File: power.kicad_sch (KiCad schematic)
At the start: 32 parts, among them J1 Conn_01x02, J2 XT30PB-M, J3 Conn_01x02, J4 Conn_01x02, Q1 IRF4905, U1 TSR3-24120N, U2 R-78E5.0-1.0, U3 TMCS1100A2QDR

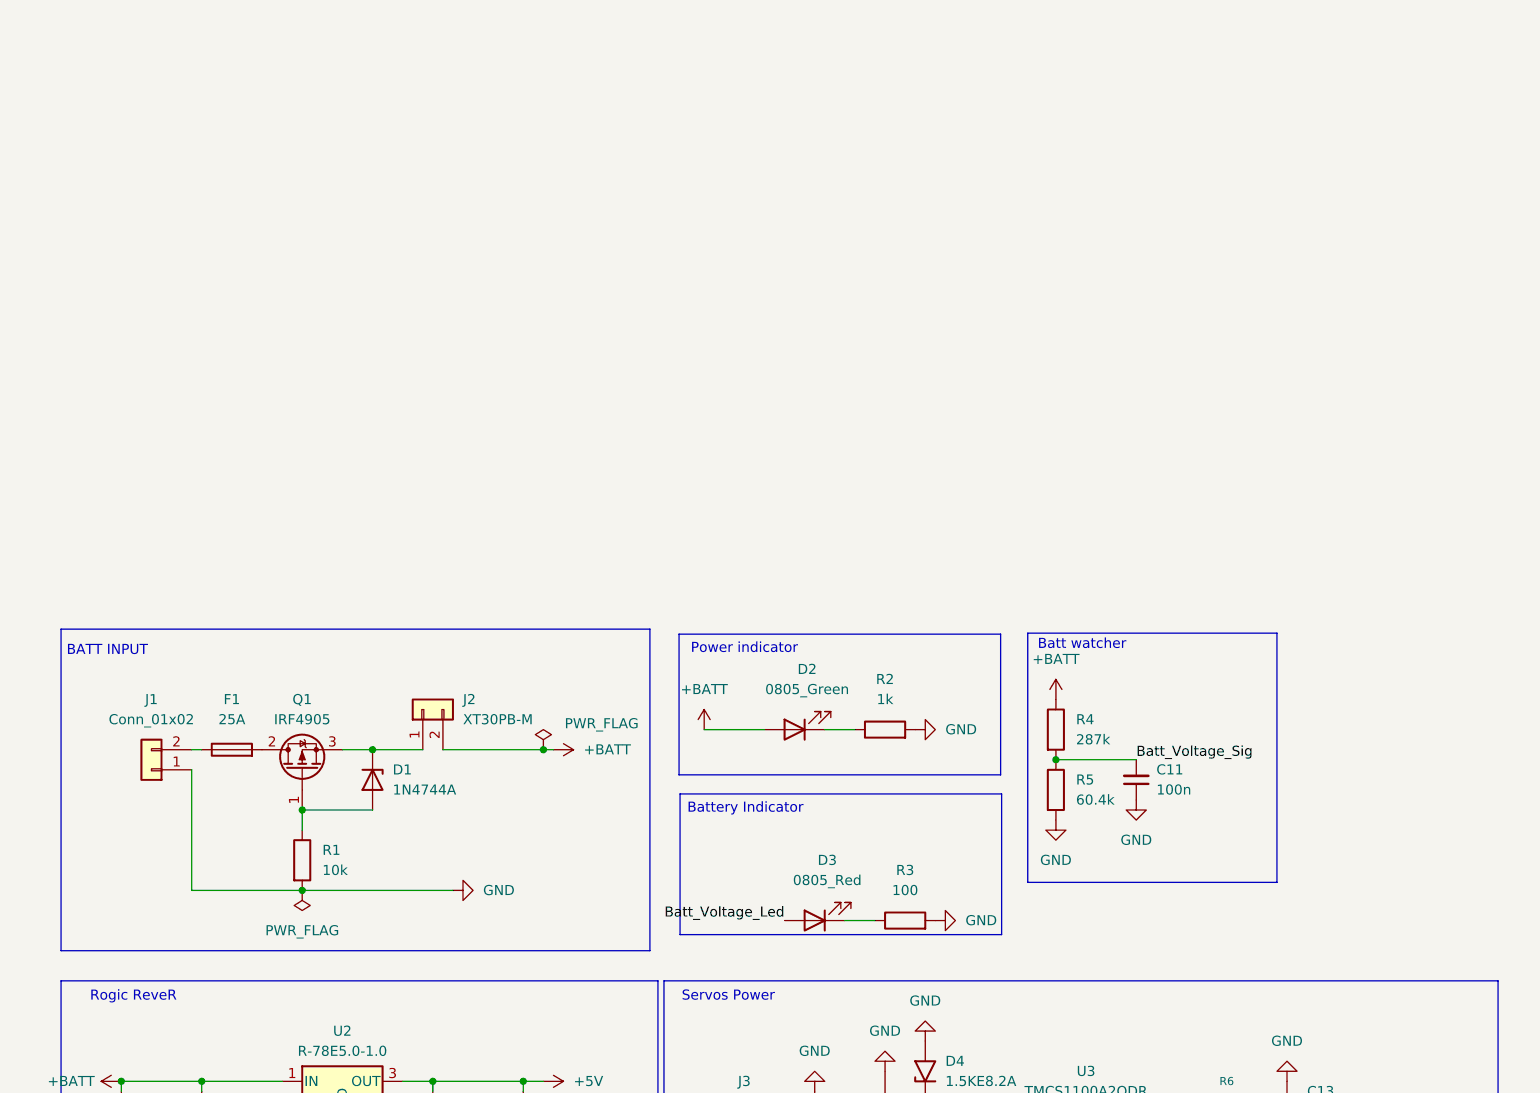
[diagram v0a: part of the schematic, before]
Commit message: Add relay for BAU + fixes
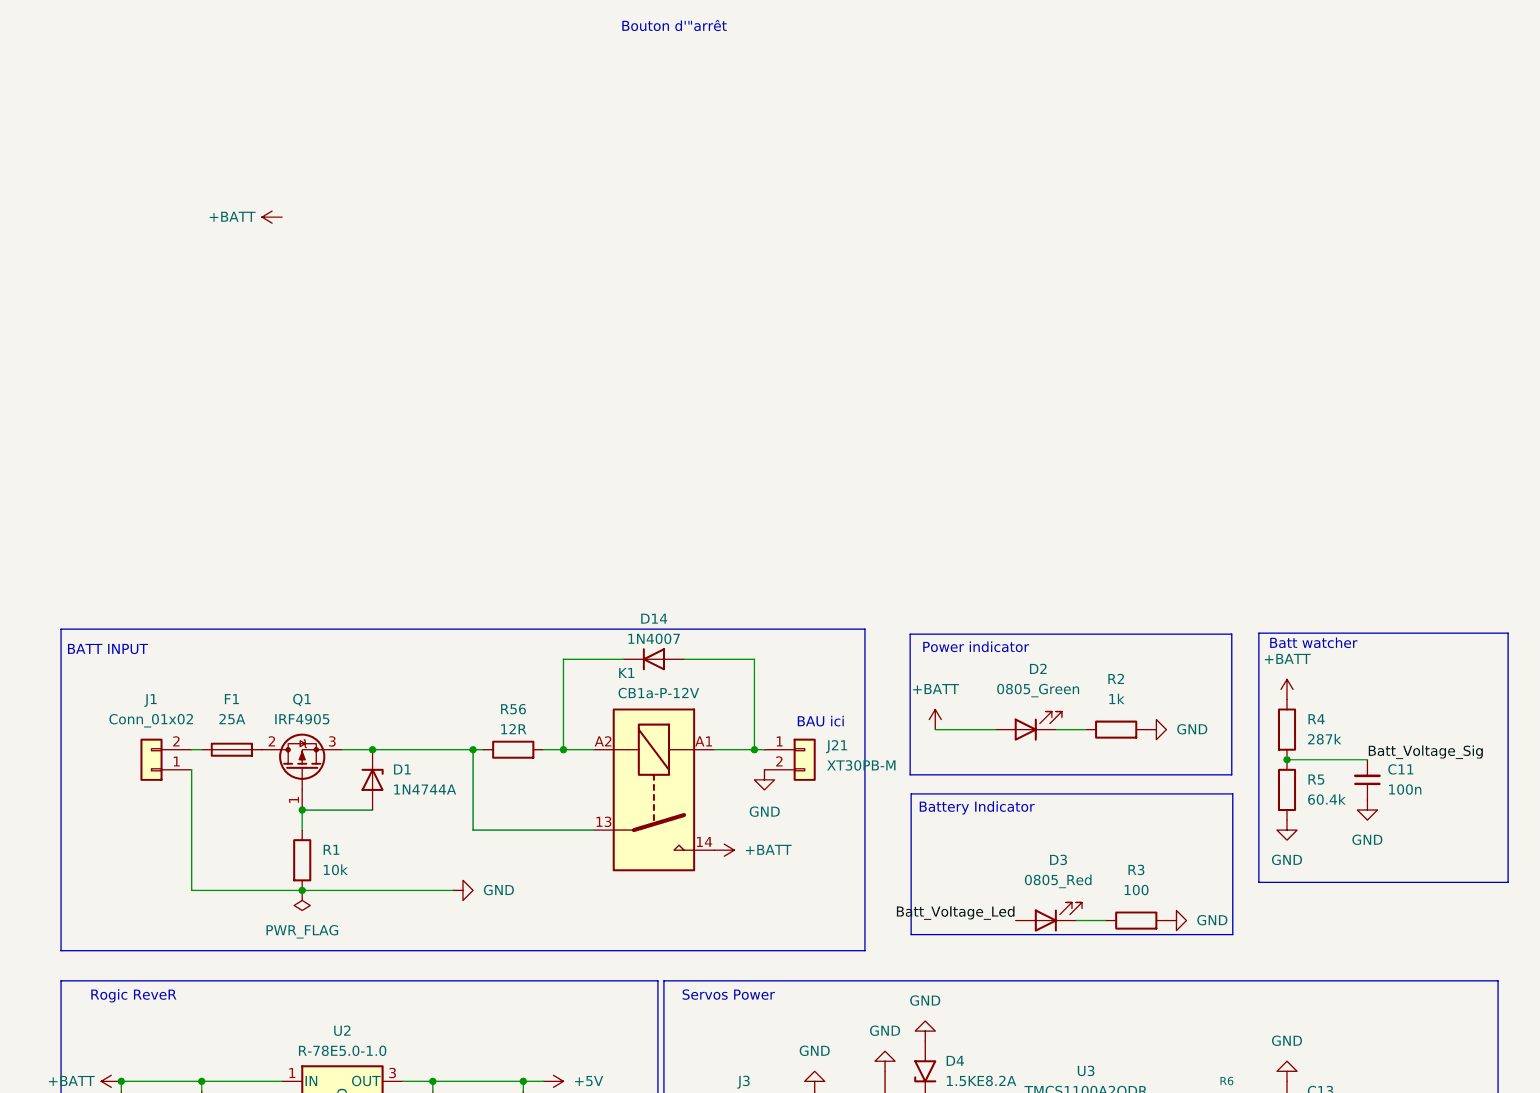
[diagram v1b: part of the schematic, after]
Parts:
- removed J2: XT30PB-M, symbol Connector_Generic:Conn_01x02
- added D14: 1N4007, symbol Device:D
- added J21: XT30PB-M, symbol Connector_Generic:Conn_01x02
- added K1: CB1a-P-12V, symbol Relay:Relay_SPST-NO
- added R56: 12R, symbol Device:R
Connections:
- net +BATT: now also K1.14
- net GND: now also J21.2 (Pin_2)
- net at D1.1 (K), Q1.3 (S): now also K1.13, R56.1
- new net: D14.2 (A), J21.1 (Pin_1), K1.A1
- new net: D14.1 (K), K1.A2, R56.2
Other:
- note added: "BAU ici"
- note added: "Bouton d'"arrêt"
- moved on the sheet: C11, D2, D3, R2, R3, R4, R5

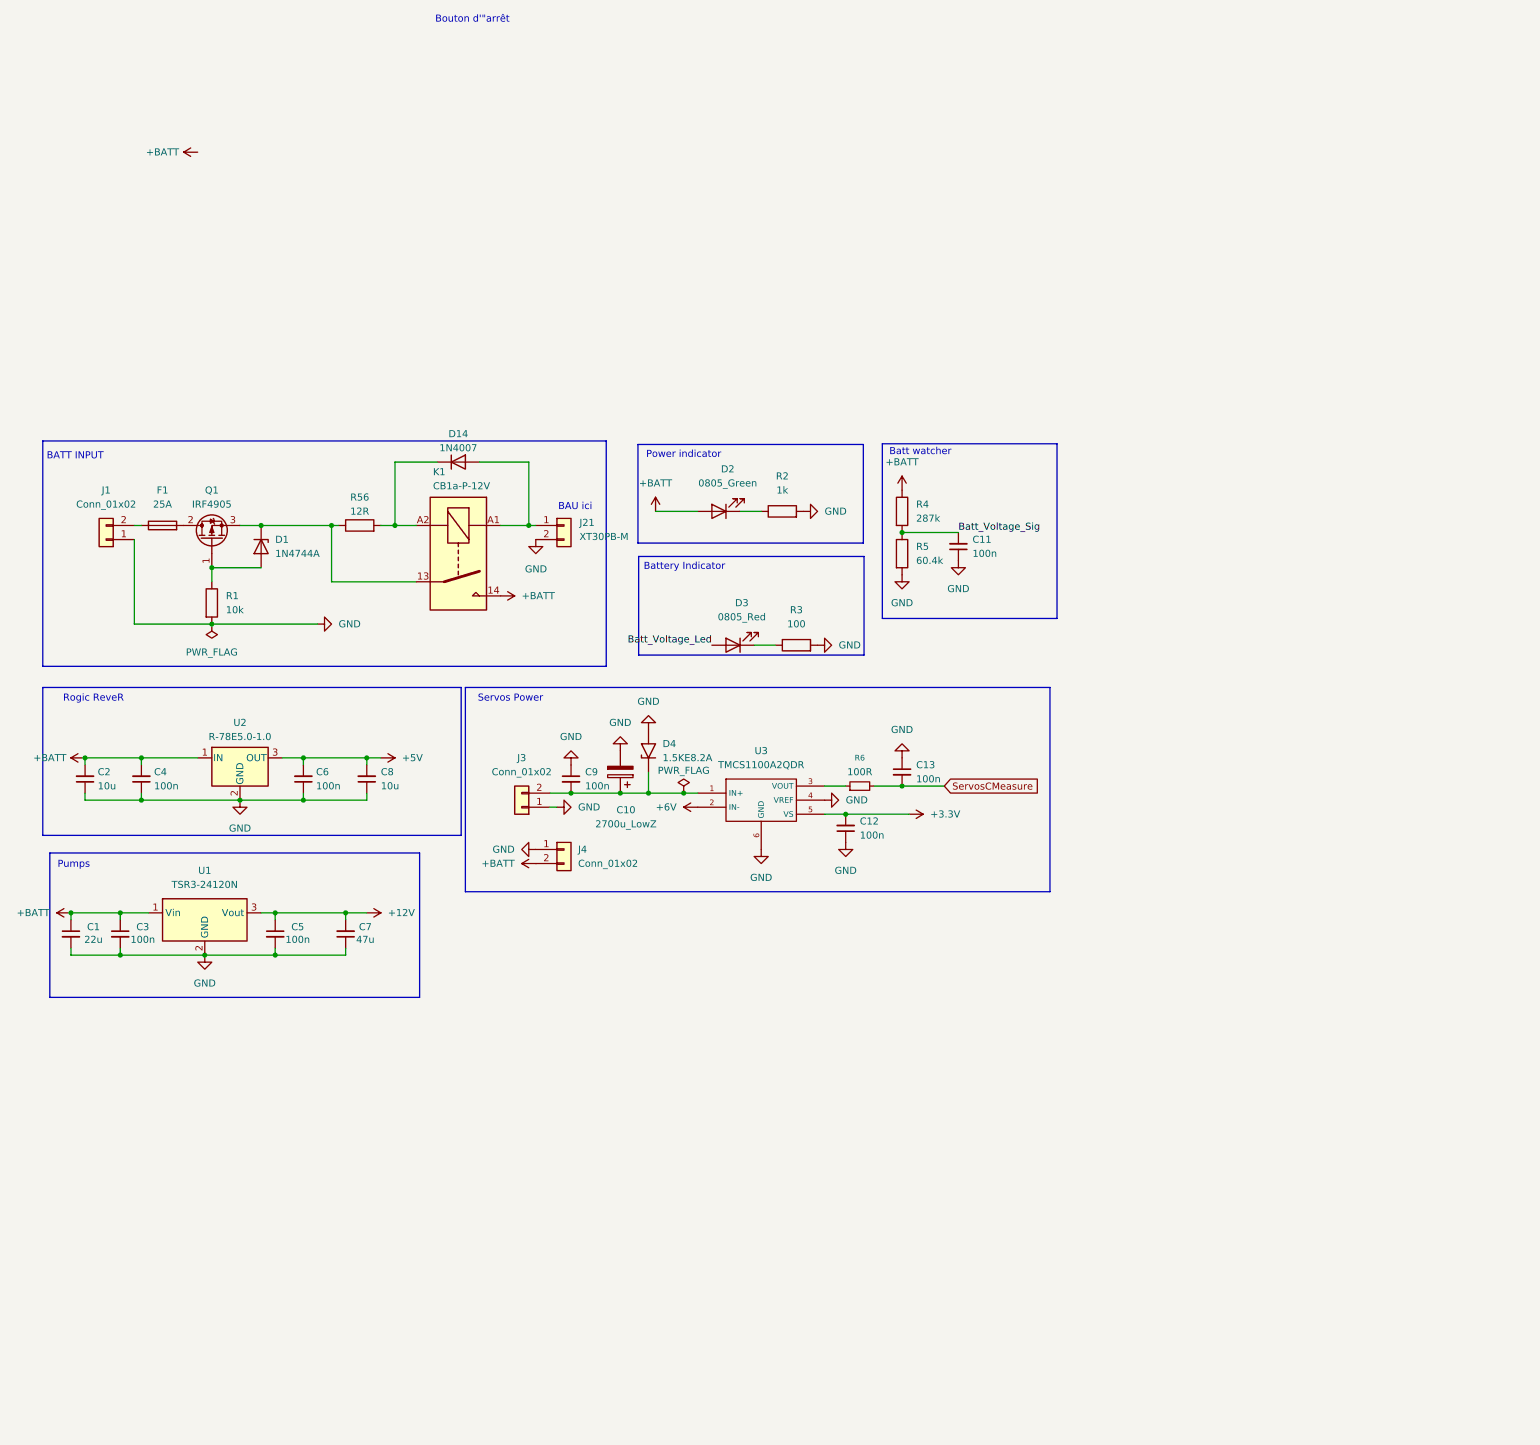
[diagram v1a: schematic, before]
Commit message: Add CB1-P-12V relay footprint, 3D model, and symbols
Added CB1-P-12V.stp 3D model and CB1P12V.kicad_mod footprint to the libs directory. Updated libs/sym.kicad_sym and multiple schematic sheets to include and reference the new relay. Adjusted eurobot-2026-robot-pcb.kicad_pro BOM and group settings to support new components.
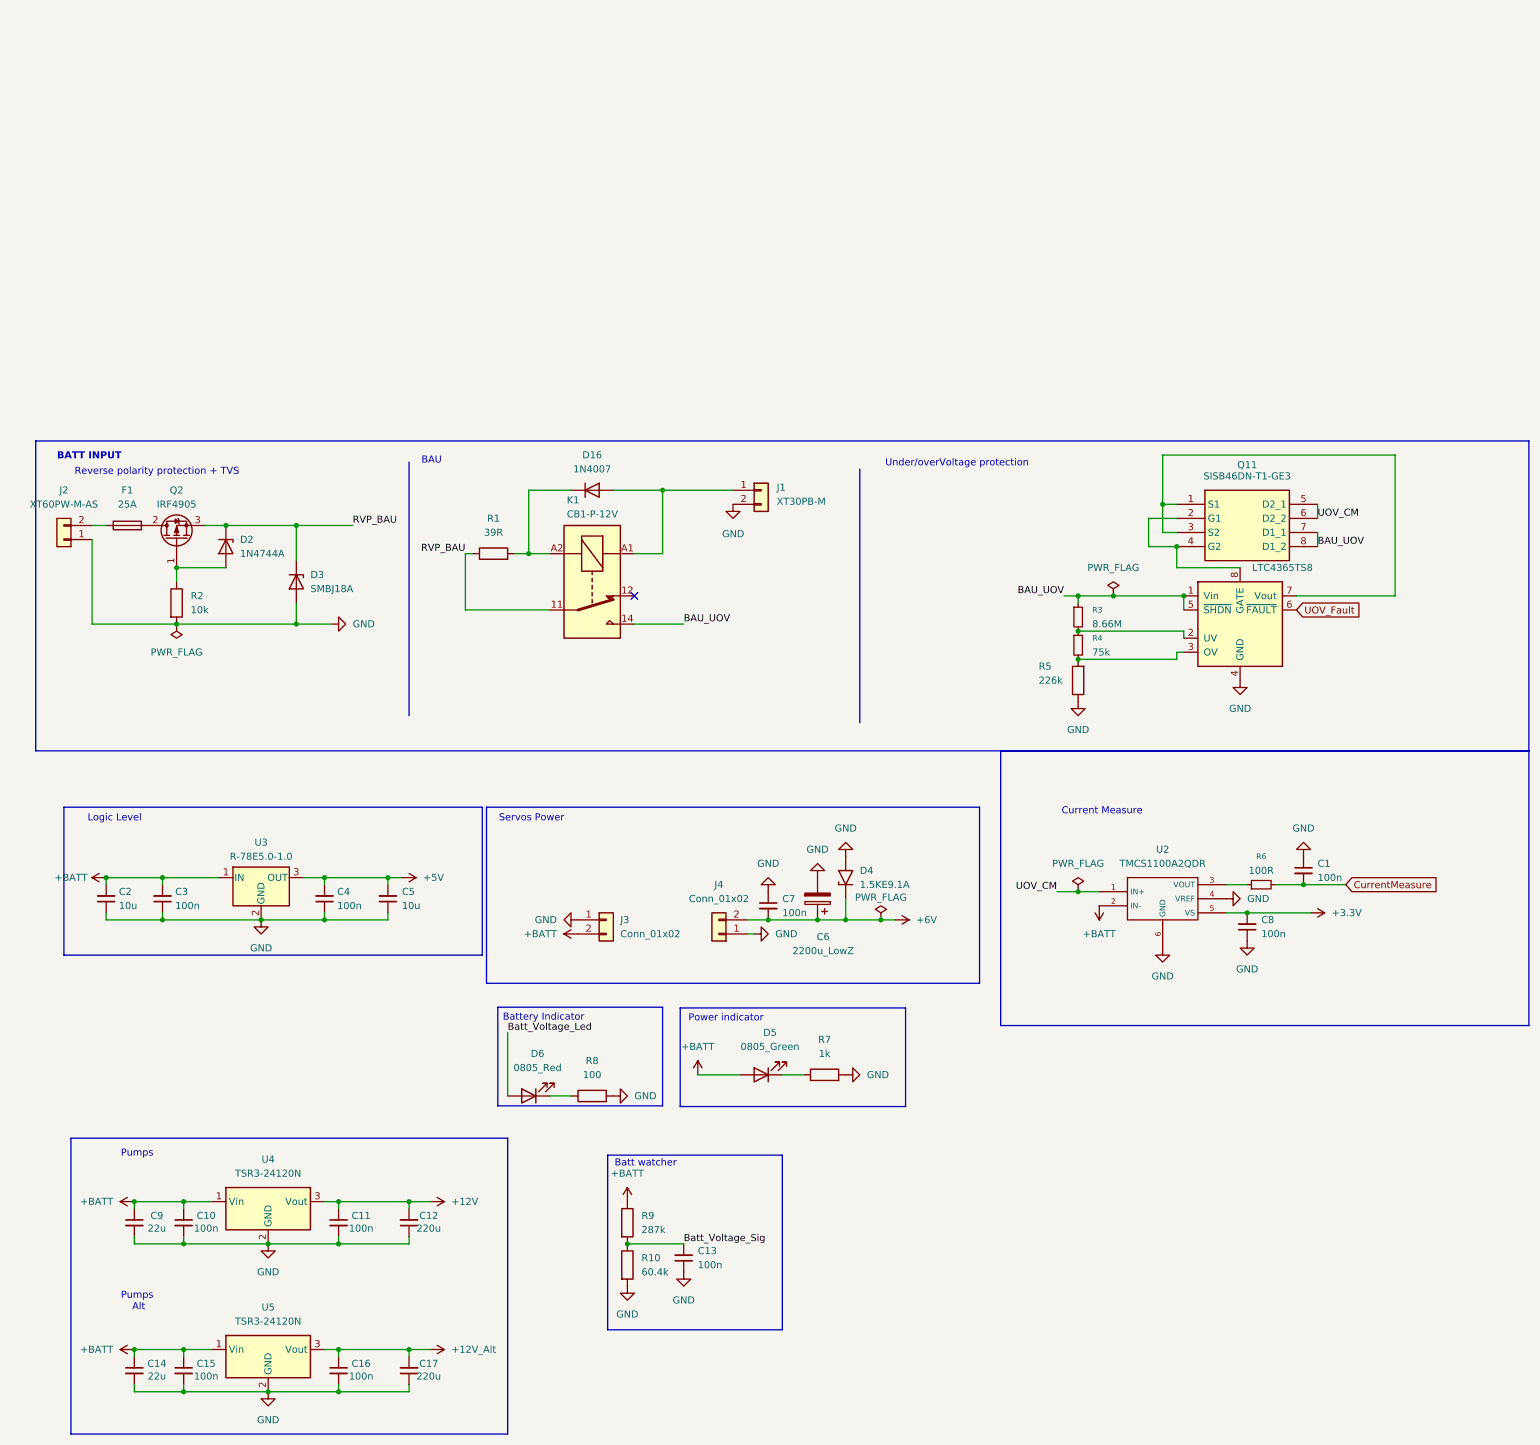
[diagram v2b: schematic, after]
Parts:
- removed C12, C13: 100n, Capacitor_SMD:C_0805_2012Metric_Pad1.18x1.45mm_HandSolder, symbol Device:C_Small
- removed D14: 1N4007, symbol Device:D
- removed U3: TMCS1100A2QDR, symbol Project:TMCS1100A2QDR
- added C1, C15, C16, C8: 100n, Capacitor_SMD:C_0805_2012Metric_Pad1.18x1.45mm_HandSolder, symbol Device:C_Small
- added C14: 22u, Capacitor_SMD:C_0805_2012Metric_Pad1.18x1.45mm_HandSolder, symbol Device:C_Small
- added C17: 220u, Capacitor_SMD:C_0805_2012Metric_Pad1.18x1.45mm_HandSolder, symbol Device:C_Small
- added D16: 1N4007, Diode_THT:D_DO-41_SOD81_P10.16mm_Horizontal, symbol Diode:1N4007
- added D3: SMBJ18A, Diode_SMD:D_SMB_Handsoldering, symbol Device:D_Zener
- added Q11: SISB46DN-T1-GE3, POWERPAK-1212-8_DUAL, symbol Project:SISB46DN-T1-GE3
- added R3: 8.66M, symbol Device:R_Small
- added R4: 75k, symbol Device:R_Small
- added R5: 226k, symbol Device:R
- added U1: LTC4365TS8, Package_TO_SOT_SMD:TSOT-23-8_HandSoldering, symbol Power_Management:LTC4365TS8
- added U2: TMCS1100A2QDR, symbol Project:TMCS1100A2QDR
- added U5: TSR3-24120N, Converter_DCDC:Converter_DCDC_TRACO_TSR2-24xxN_TSR2-24xxxN_THT, symbol Regulator_Switching:TSR3-24120N
- C12: renamed from C7; value 47u -> 220u
- C6: renamed from C10; value 2700u_LowZ -> 2200u_LowZ; footprint Capacitor_THT:CP_Radial_D8.0mm_P3.50mm -> Capacitor_THT:CP_Radial_D12.5mm_P5.00mm; MPN EEU-FR1E272L -> EEUFR1C222
- D4: value 1.5KE8.2A -> 1.5KE9.1A
- J2: renamed from J1; value Conn_01x02 -> XT60PW-M-AS
- K1: value CB1a-P-12V -> CB1-P-12V; footprint (none) -> Project:CB1P12V; symbol Relay:Relay_SPST-NO -> Relay:Relay_SPDT
- R1: renamed from R56; value 12R -> 39R; footprint (none) -> Resistor_SMD:R_2512_6332Metric_Pad1.40x3.35mm_HandSolder
- R2: renamed from R1; footprint (none) -> Resistor_SMD:R_0805_2012Metric_Pad1.20x1.40mm_HandSolder
- renumbered C3 to C10, C5 to C11, C11 to C13, C4 to C3, C6 to C4, C8 to C5, C9 to C7, C1 to C9, D1 to D2, D2 to D5, D3 to D6, J21 to J1, J4 to J3, J3 to J4, Q1 to Q2, R5 to R10, R2 to R7, R3 to R8, R4 to R9, U2 to U3, U1 to U4
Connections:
- net +3.3V: now also C8.2, U2.5 (VS)
- net +6V: now also C6.1, C7.2, D4.1 (A1), J4.2 (Pin_2)
- net +BATT: now also C14.1, C15.1, U2.2 (IN-), U5.1 (Vin); no longer K1.14
- net GND: now also C1.1, C14.2, C15.2, C16.2, C17.1, C8.1, D3.2 (A), R5.1, U1.4 (GND), U2.4 (VREF), U2.6 (GND), U5.2 (GND)
- net at R6.1: now also U2.3 (VOUT)
- net RVP_BAU: now reaches D2.1 (K), Q2.3 (S), R1.1
- net RVP_BAU: now also K1.11, D3.1 (K); no longer K1.13
- net at J1.1 (Pin_1), K1.A1: now also D16.2 (A)
- net at K1.A2, R1.2: now also D16.1 (K)
- net ServosCMeasure renamed CurrentMeasure
- net CurrentMeasure: now also C1.2
- new net: R3.2, R4.1, U1.2 (UV)
- new net: R4.2, R5.2, U1.3 (OV)
- new net: Q11.1 (S1), Q11.3 (S2), U1.7 (Vout)
- new net: Q11.2 (G1), Q11.4 (G2), U1.8 (GATE)
- new net +12V_Alt: C16.1, C17.2, U5.3 (Vout)
- new net BAU_UOV: K1.14, Q11.7 (D1_1), Q11.8 (D1_2), R3.1, U1.1 (Vin), U1.5 (~{SHDN})
- new net UOV_CM: Q11.5 (D2_1), Q11.6 (D2_2), U2.1 (IN+)
- new net UOV_Fault: U1.6 (~{FAULT})
- no-connect marks 0 -> 1
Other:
- note added: "BAU"
- note added: "Current Measure"
- note added: "Logic Level"
- note added: "Pumps Alt"
- note added: "Reverse polarity protection + TVS"
- note added: "Under/overVoltage protection"
- note removed: "BAU ici"
- note removed: "Bouton d'"arrêt"
- note removed: "Rogic ReveR"
- moved on the sheet: C10, C11, C12, C13, C2, C3, C4, C5, C6, C7, C9, D2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
